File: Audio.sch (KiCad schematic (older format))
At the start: 41 parts, among them J1 AUDIO JACK, J2 JACK_TRS_4PINS, J3 AUDIO JACK, J4 AUDIO JACK, U10 TLV320AIC3104, U11 TPA2010D1

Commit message: just added NOTE field to BOMS AWAY
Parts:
- C116, C145, C33, C35, C37: SPN (none) -> 490-1709-1-ND; SPR (none) -> Digikey
- C117, C143, C27, C28, C30, C32, C34, C36, C38, C39, C40: SPN (none) -> 490-1532-1-ND; SPR (none) -> Digikey
- C144, C147: SPN (none) -> 478-8139-1-ND; SPR (none) -> Digikey
- C152: SPN (none) -> 490-10451-1-ND; SPR (none) -> Digikey
- C26: SPN (none) -> 490-9750-1-ND; SPR (none) -> Digikey
- U11: MFR (none) -> Texas Instruments; MPN (none) -> TPA2010D1YZFR; SPN (none) -> 296-16648-1-ND; SPR (none) -> Digikey
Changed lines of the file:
@@
 F 4 "Murata" H 0 0 50 0001 C CNN "MFR"
 F 5 "GRM188R71C104KA01D" H 0 0 50 0001 C CNN "MPN"
-F 6 "" H 0 0 50 0001 C CNN "SPR"
-F 7 "" H 0 0 50 0001 C CNN "SPN"
+F 6 "Digikey" H 0 0 50 0001 C CNN "SPR"
+F 7 "490-1532-1-ND" H 0 0 50 0001 C CNN "SPN"
 F 8 "" H 0 0 50 0001 C CNN "SPURL"
 	1    2400 3550
@@
 F 4 "Murata" H 0 0 50 0001 C CNN "MFR"
 F 5 "GRM188R71C104KA01D" H 0 0 50 0001 C CNN "MPN"
-F 6 "" H 0 0 50 0001 C CNN "SPR"
-F 7 "" H 0 0 50 0001 C CNN "SPN"
+F 6 "Digikey" H 0 0 50 0001 C CNN "SPR"
+F 7 "490-1532-1-ND" H 0 0 50 0001 C CNN "SPN"
 F 8 "" H 0 0 50 0001 C CNN "SPURL"
 	1    10600 2250
@@
 F 4 "Murata" H 0 0 50 0001 C CNN "MFR"
 F 5 "GRM188R71C104KA01D" H 0 0 50 0001 C CNN "MPN"
-F 6 "" H 0 0 50 0001 C CNN "SPR"
-F 7 "" H 0 0 50 0001 C CNN "SPN"
+F 6 "Digikey" H 0 0 50 0001 C CNN "SPR"
+F 7 "490-1532-1-ND" H 0 0 50 0001 C CNN "SPN"
 F 8 "" H 0 0 50 0001 C CNN "SPURL"
 	1    10750 3550
@@
 F 4 "Murata" H 0 0 50 0001 C CNN "MFR"
 F 5 "GRM188R71C104KA01D" H 0 0 50 0001 C CNN "MPN"
-F 6 "" H 0 0 50 0001 C CNN "SPR"
-F 7 "" H 0 0 50 0001 C CNN "SPN"
+F 6 "Digikey" H 0 0 50 0001 C CNN "SPR"
+F 7 "490-1532-1-ND" H 0 0 50 0001 C CNN "SPN"
 F 8 "" H 0 0 50 0001 C CNN "SPURL"
 	1    9400 4850
@@
 F 4 "Murata" H 0 0 50 0001 C CNN "MFR"
 F 5 "GRM21BR61A475KA73L" H 0 0 50 0001 C CNN "MPN"
-F 6 "" H 0 0 50 0001 C CNN "SPR"
-F 7 "" H 0 0 50 0001 C CNN "SPN"
+F 6 "Digikey" H 0 0 50 0001 C CNN "SPR"
+F 7 "490-9750-1-ND" H 0 0 50 0001 C CNN "SPN"
 F 8 "" H 0 0 50 0001 C CNN "SPURL"
 	1    3900 4800
@@
 F 4 "Murata" H 0 0 50 0001 C CNN "MFR"
 F 5 "GRM188R71C104KA01D" H 0 0 50 0001 C CNN "MPN"
-F 6 "" H 0 0 50 0001 C CNN "SPR"
-F 7 "" H 0 0 50 0001 C CNN "SPN"
+F 6 "Digikey" H 0 0 50 0001 C CNN "SPR"
+F 7 "490-1532-1-ND" H 0 0 50 0001 C CNN "SPN"
 F 8 "" H 0 0 50 0001 C CNN "SPURL"
 	1    7050 4650
@@
 F 4 "Murata" H 0 0 50 0001 C CNN "MFR"
 F 5 "GRM188R71C104KA01D" H 0 0 50 0001 C CNN "MPN"
-F 6 "" H 0 0 50 0001 C CNN "SPR"
-F 7 "" H 0 0 50 0001 C CNN "SPN"
+F 6 "Digikey" H 0 0 50 0001 C CNN "SPR"
+F 7 "490-1532-1-ND" H 0 0 50 0001 C CNN "SPN"
 F 8 "" H 0 0 50 0001 C CNN "SPURL"
 	1    7500 4550
@@
 F 4 "Murata" H 0 0 50 0001 C CNN "MFR"
 F 5 "GRM21BR61A106KE19L" H 0 0 50 0001 C CNN "MPN"
-F 6 "" H 0 0 50 0001 C CNN "SPR"
-F 7 "" H 0 0 50 0001 C CNN "SPN"
+F 6 "Digikey" H 0 0 50 0001 C CNN "SPR"
+F 7 "490-1709-1-ND" H 0 0 50 0001 C CNN "SPN"
 F 8 "" H 0 0 50 0001 C CNN "SPURL"
 	1    7250 4650
@@
 F 4 "Murata" H 0 0 50 0001 C CNN "MFR"
 F 5 "GRM21BR61A106KE19L" H 0 0 50 0001 C CNN "MPN"
-F 6 "" H 0 0 50 0001 C CNN "SPR"
-F 7 "" H 0 0 50 0001 C CNN "SPN"
+F 6 "Digikey" H 0 0 50 0001 C CNN "SPR"
+F 7 "490-1709-1-ND" H 0 0 50 0001 C CNN "SPN"
 F 8 "" H 0 0 50 0001 C CNN "SPURL"
 	1    7700 4550
@@
 F 4 "Murata" H 0 0 50 0001 C CNN "MFR"
 F 5 "GRM188R71C104KA01D" H 0 0 50 0001 C CNN "MPN"
-F 6 "" H 0 0 50 0001 C CNN "SPR"
-F 7 "" H 0 0 50 0001 C CNN "SPN"
+F 6 "Digikey" H 0 0 50 0001 C CNN "SPR"
+F 7 "490-1532-1-ND" H 0 0 50 0001 C CNN "SPN"
 F 8 "" H 0 0 50 0001 C CNN "SPURL"
 	1    7250 3150
@@
 F 4 "Murata" H 0 0 50 0001 C CNN "MFR"
 F 5 "GRM21BR61A106KE19L" H 0 0 50 0001 C CNN "MPN"
-F 6 "" H 0 0 50 0001 C CNN "SPR"
-F 7 "" H 0 0 50 0001 C CNN "SPN"
+F 6 "Digikey" H 0 0 50 0001 C CNN "SPR"
+F 7 "490-1709-1-ND" H 0 0 50 0001 C CNN "SPN"
 F 8 "" H 0 0 50 0001 C CNN "SPURL"
 	1    7050 3150
@@
 F 4 "Murata" H 0 0 50 0001 C CNN "MFR"
 F 5 "GRM188R71C104KA01D" H 0 0 50 0001 C CNN "MPN"
-F 6 "" H 0 0 50 0001 C CNN "SPR"
-F 7 "" H 0 0 50 0001 C CNN "SPN"
+F 6 "Digikey" H 0 0 50 0001 C CNN "SPR"
+F 7 "490-1532-1-ND" H 0 0 50 0001 C CNN "SPN"
 F 8 "" H 0 0 50 0001 C CNN "SPURL"
 	1    8100 4450
@@
 F 4 "Murata" H 0 0 50 0001 C CNN "MFR"
 F 5 "GRM188R71C104KA01D" H 0 0 50 0001 C CNN "MPN"
-F 6 "" H 0 0 50 0001 C CNN "SPR"
-F 7 "" H 0 0 50 0001 C CNN "SPN"
+F 6 "Digikey" H 0 0 50 0001 C CNN "SPR"
+F 7 "490-1532-1-ND" H 0 0 50 0001 C CNN "SPN"
 F 8 "" H 0 0 50 0001 C CNN "SPURL"
 	1    3200 3350
@@
 F 4 "Murata" H 0 0 50 0001 C CNN "MFR"
 F 5 "GRM21BR61A106KE19L" H 0 0 50 0001 C CNN "MPN"
-F 6 "" H 0 0 50 0001 C CNN "SPR"
-F 7 "" H 0 0 50 0001 C CNN "SPN"
+F 6 "Digikey" H 0 0 50 0001 C CNN "SPR"
+F 7 "490-1709-1-ND" H 0 0 50 0001 C CNN "SPN"
 F 8 "" H 0 0 50 0001 C CNN "SPURL"
 	1    3400 3350
@@
 F 4 "Murata" H 0 0 50 0001 C CNN "MFR"
 F 5 "GRM155R61A225KE95D" H 0 0 50 0001 C CNN "MPN"
-F 6 "" H 0 0 50 0001 C CNN "SPR"
-F 7 "" H 0 0 50 0001 C CNN "SPN"
+F 6 "Digikey" H 0 0 50 0001 C CNN "SPR"
+F 7 "490-10451-1-ND" H 0 0 50 0001 C CNN "SPN"
 F 8 "" H 0 0 50 0001 C CNN "SPURL"
 	1    2750 5000
@@
 F 4 "AVX Corporation" H 0 0 50 0001 C CNN "MFR"
 F 5 "F930G227KBA" H 0 0 50 0001 C CNN "MPN"
-F 6 "" H 0 0 50 0001 C CNN "SPR"
-F 7 "" H 0 0 50 0001 C CNN "SPN"
+F 6 "Digikey" H 0 0 50 0001 C CNN "SPR"
+F 7 "478-8139-1-ND" H 0 0 50 0001 C CNN "SPN"
 F 8 "" H 0 0 50 0001 C CNN "SPURL"
 	1    9000 5400
@@
 F 4 "AVX Corporation" H 0 0 50 0001 C CNN "MFR"
 F 5 "F930G227KBA" H 0 0 50 0001 C CNN "MPN"
-F 6 "" H 0 0 50 0001 C CNN "SPR"
-F 7 "" H 0 0 50 0001 C CNN "SPN"
+F 6 "Digikey" H 0 0 50 0001 C CNN "SPR"
+F 7 "478-8139-1-ND" H 0 0 50 0001 C CNN "SPN"
 F 8 "" H 0 0 50 0001 C CNN "SPURL"
 	1    8500 5600
@@
 F 4 "Murata" H 0 0 50 0001 C CNN "MFR"
 F 5 "GRM21BR61A106KE19L" H 0 0 50 0001 C CNN "MPN"
-F 6 "" H 0 0 50 0001 C CNN "SPR"
-F 7 "" H 0 0 50 0001 C CNN "SPN"
+F 6 "Digikey" H 0 0 50 0001 C CNN "SPR"
+F 7 "490-1709-1-ND" H 0 0 50 0001 C CNN "SPN"
 F 8 "" H 0 0 50 0001 C CNN "SPURL"
 	1    7900 4450
@@
 F 2 "DFTcustom:9DSBGA" H 10150 4700 60 0001 C CNN
 F 3 "" H 10150 4700 60 0001 C CNN
-F 4 "" H 0 0 50 0001 C CNN "MFR"
-F 5 "" H 0 0 50 0001 C CNN "MPN"
-F 6 "" H 0 0 50 0001 C CNN "SPR"
-F 7 "" H 0 0 50 0001 C CNN "SPN"
+F 4 "Texas Instruments" H 0 0 50 0001 C CNN "MFR"
+F 5 "TPA2010D1YZFR" H 0 0 50 0001 C CNN "MPN"
+F 6 "Digikey" H 0 0 50 0001 C CNN "SPR"
+F 7 "296-16648-1-ND" H 0 0 50 0001 C CNN "SPN"
 F 8 "" H 0 0 50 0001 C CNN "SPURL"
 	1    10150 4700
@@
 F 4 "Murata" H 0 0 50 0001 C CNN "MFR"
 F 5 "GRM188R71C104KA01D" H 0 0 50 0001 C CNN "MPN"
-F 6 "" H 0 0 50 0001 C CNN "SPR"
-F 7 "" H 0 0 50 0001 C CNN "SPN"
+F 6 "Digikey" H 0 0 50 0001 C CNN "SPR"
+F 7 "490-1532-1-ND" H 0 0 50 0001 C CNN "SPN"
 F 8 "" H 0 0 50 0001 C CNN "SPURL"
 	1    9100 4000
@@
 F 4 "Murata" H 0 0 50 0001 C CNN "MFR"
 F 5 "GRM188R71C104KA01D" H 0 0 50 0001 C CNN "MPN"
-F 6 "" H 0 0 50 0001 C CNN "SPR"
-F 7 "" H 0 0 50 0001 C CNN "SPN"
+F 6 "Digikey" H 0 0 50 0001 C CNN "SPR"
+F 7 "490-1532-1-ND" H 0 0 50 0001 C CNN "SPN"
 F 8 "" H 0 0 50 0001 C CNN "SPURL"
 	1    8850 4250

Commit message: Complete BOM. all resistors now 0402
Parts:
- J1, J3, J4: SPN (none) -> SC2083-ND; SPR (none) -> Digikey
- J2: MFR (none) -> CUI Inc.; MPN (none) -> SJ-3524-SMT-TR; SPN (none) -> CP-3524SJCT-ND; SPR (none) -> Digikey
- MIC1: SPN (none) -> WM7121PIMSE/RVCT-ND; SPR (none) -> Digikey
- R34, R37, R38, R39: footprint Resistors_SMD:R_0603 -> Resistors_SMD:R_0402; MFR Vishay Dale -> Yageo; MPN CRCW0603100KFKEA -> RC0402FR-07100KL; SPN (none) -> 311-100KLRTR-ND; SPR (none) -> Digikey
- R35, R40, R41, R42: MFR Vishay Dale -> Yageo; MPN CRCW040249K9FKED -> RC0402FR-0749K9L; SPN (none) -> 311-49.9KLRCT-ND; SPR (none) -> Digikey
- R36, R44: MFR (none) -> Yageo; MPN (none) -> RC0402FR-0715KL; SPN (none) -> 311-15.0KLRCT-ND; SPR (none) -> Digikey
- R54: MFR Vishay Dale -> Yageo; MPN CRCW04024K70FKED -> RC0402FR-074K7L; SPN (none) -> 311-4.7KLRCT-ND; SPR (none) -> Digikey
- U10: MFR (none) -> Texas Instruments; MPN (none) -> TLV320AIC3104IRHBR; SPN (none) -> 296-26818-1-ND; SPR (none) -> Digikey

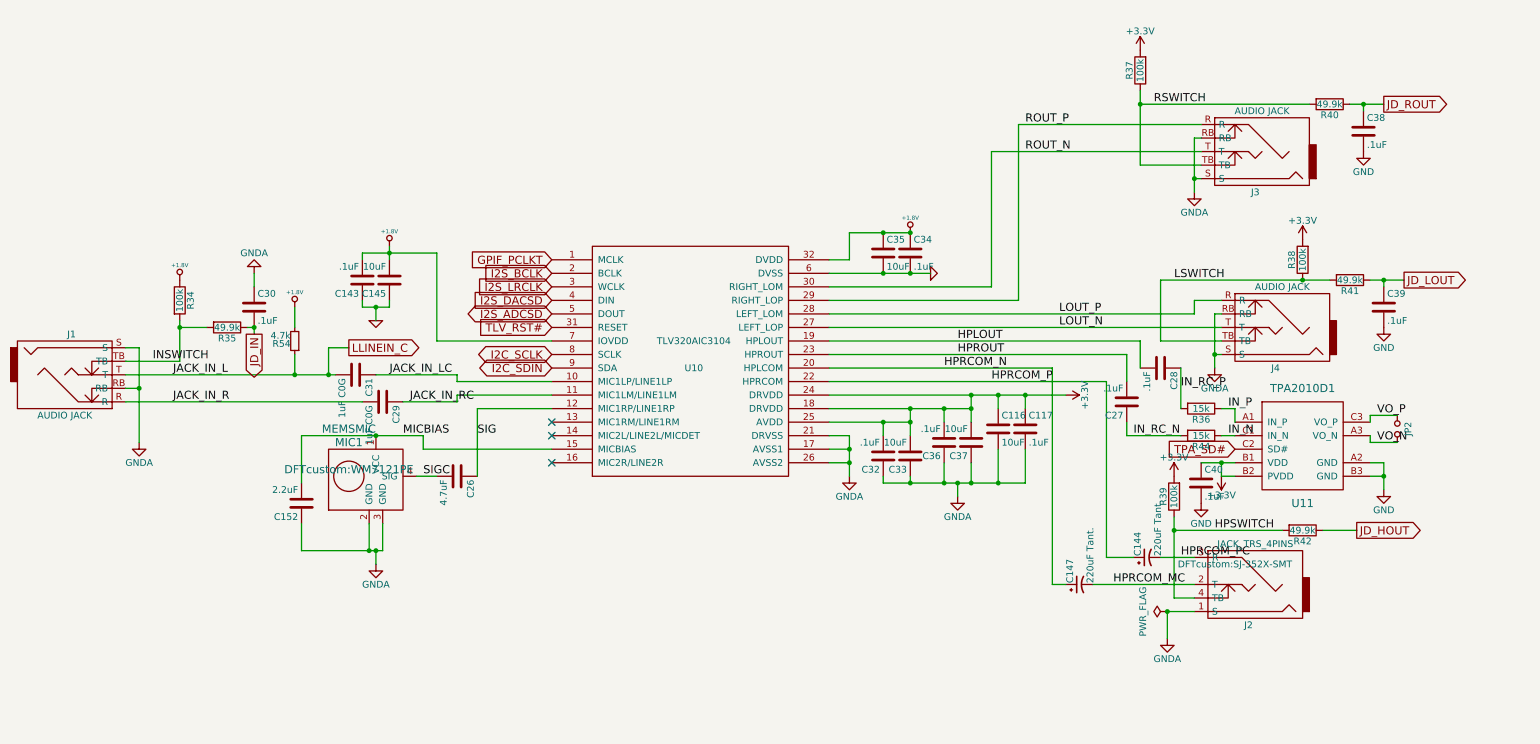
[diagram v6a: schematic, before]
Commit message: added caps to audio
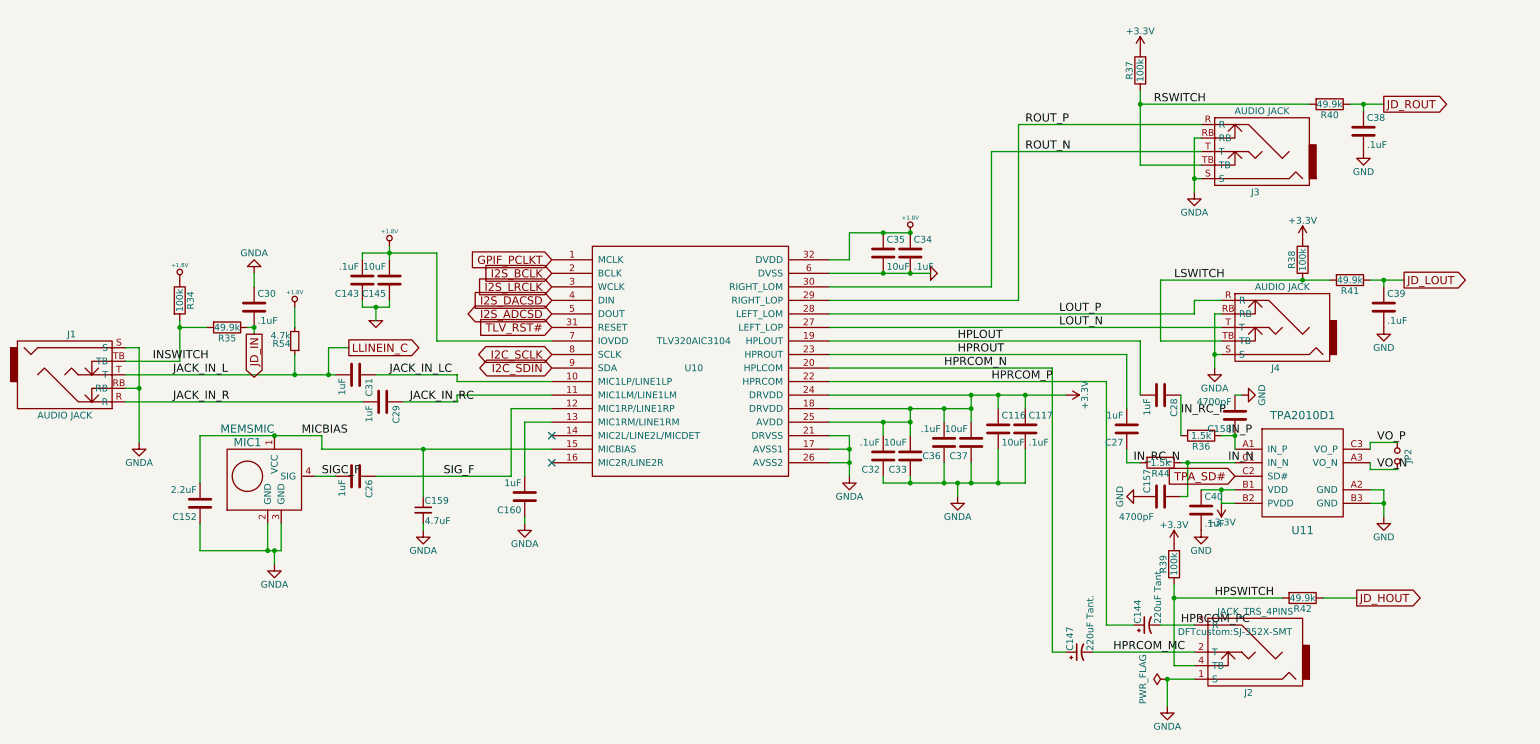
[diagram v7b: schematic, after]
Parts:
- added C157, C158: 4700pF, Capacitors_SMD:C_0603, symbol C
- added C159: 4.7uF, Capacitors_SMD:C_0805, symbol C_Small
- added C160: 1uF, Capacitors_SMD:C_0603, symbol C
- C26: value 4.7uF -> 1uF; footprint Capacitors_SMD:C_0805 -> Capacitors_SMD:C_0603; MPN GRM21BR61A475KA73L -> GRM188R71C105KE15D; SPN 490-9750-1-ND -> 490-10734-1-ND
- C27, C28: value .1uF -> 1uF; MPN GRM188R71C104KA01D -> GRM188R71C105KE15D; SPN 490-1532-1-ND -> 490-10734-1-ND
- C29, C31: value 1uF C0G -> 1uF; footprint Capacitors_SMD:C_0402 -> Capacitors_SMD:C_0603; MFR (none) -> Murata; MPN (none) -> GRM188R71C105KE15D; SPN (none) -> 490-10734-1-ND; SPR (none) -> Digikey
- R36, R44: value 15k -> 1.5k; MFR Yageo -> (none); MPN RC0402FR-0715KL -> (none); SPN 311-15.0KLRCT-ND -> (none)
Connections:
- net GND: now also C157.1, C158.2
- net GNDA: now also C159.2, C160.1
- net IN_N: now also C157.2
- net IN_P: now also C158.1
- net MICBIAS: now also C159.1
- net at U10.13 (MIC1RM/LINE1RM): now also C160.2
- net SIG renamed SIG_F
- net SIGC renamed SIGC_F
- no-connect marks 3 -> 2
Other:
- moved on the sheet: C144, C147, C152, C40, J2, JP2, MIC1, R36, R39, R42, U11
